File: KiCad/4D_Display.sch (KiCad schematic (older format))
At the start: 5 parts, among them J12 Display Serial Header, J4 V2 Display Ribbon Cable, Q3 MMBT3904

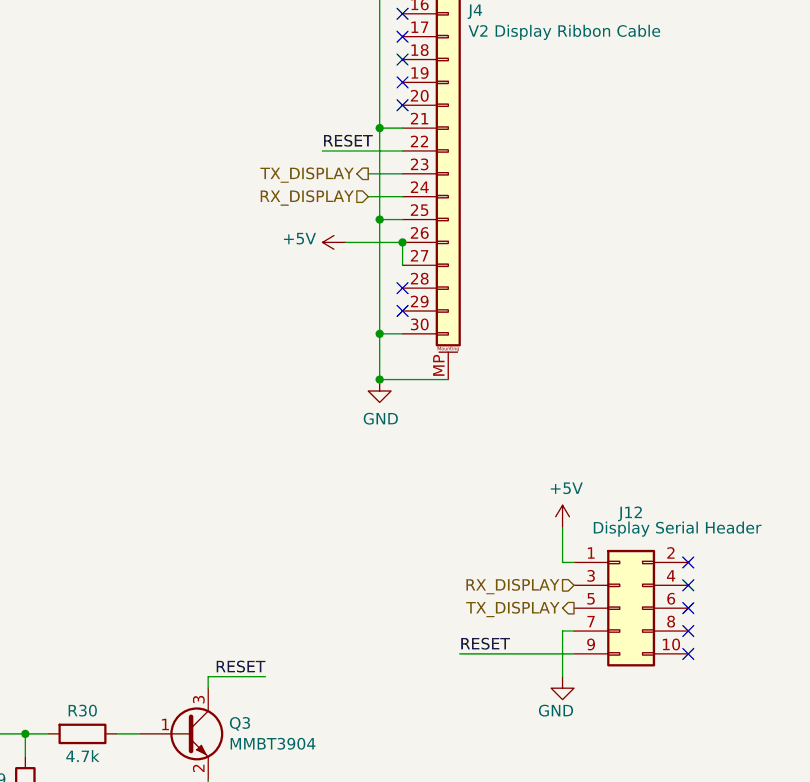
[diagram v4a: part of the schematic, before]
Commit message: Updating board to remove EXP1/EXP2
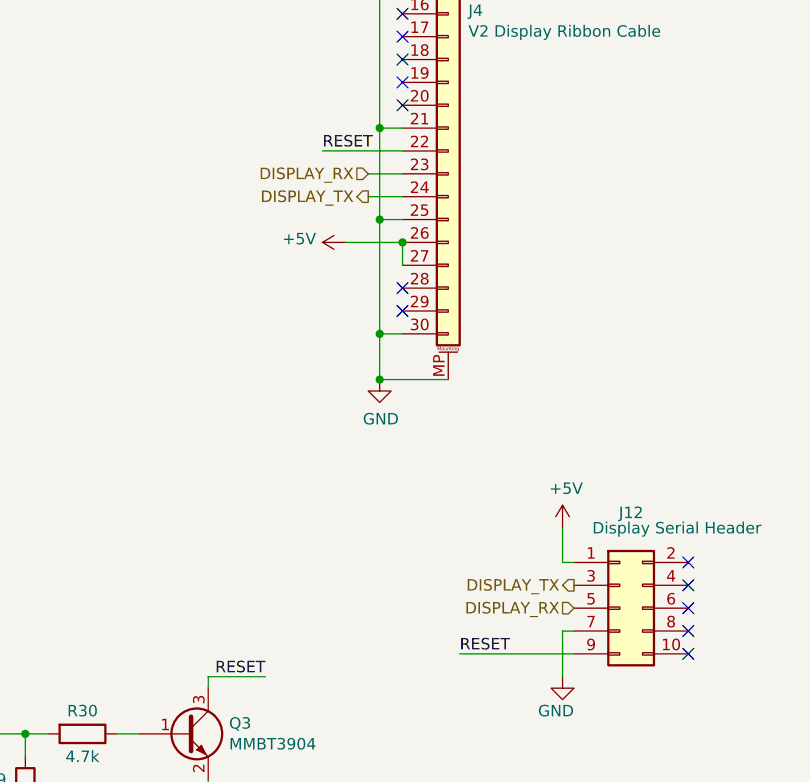
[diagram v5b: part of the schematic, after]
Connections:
- net RX_DISPLAY renamed DISPLAY_TX
- net TX_DISPLAY renamed DISPLAY_RX
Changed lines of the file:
@@
 Wire Wire Line
 	3550 6450 3550 6550
-Text HLabel 5150 5600 0    50   Input ~ 0
-RX_DISPLAY
-Text HLabel 5150 5700 0    50   Output ~ 0
-TX_DISPLAY
 Text HLabel 2350 6250 0    50   Input ~ 0
 RESET_DISPLAY
@@
 	0    -1   -1   0
 $EndComp
-Text HLabel 4250 3900 0    50   Input ~ 0
-RX_DISPLAY
-Text HLabel 4250 3800 0    50   Output ~ 0
-TX_DISPLAY
+Text HLabel 4250 3800 0    50   Input ~ 0
+DISPLAY_RX
+Text HLabel 4250 3900 0    50   Output ~ 0
+DISPLAY_TX
+Text HLabel 5150 5700 0    50   Input ~ 0
+DISPLAY_RX
+Text HLabel 5150 5600 0    50   Output ~ 0
+DISPLAY_TX
 $EndSCHEMATC

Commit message: current KiCad progress
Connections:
- net RESET_DISPLAY renamed DISPLAY_RESET
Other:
- note added: "Check: Display reset is now 3.3V,\nwill this still work on the N-channel mosfet?"
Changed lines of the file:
@@
 $Descr A4 11693 8268
 encoding utf-8
-Sheet 5 5
+Sheet 2 4
 Title ""
 Date ""
@@
 Wire Wire Line
 	3550 6450 3550 6550
-Text HLabel 2350 6250 0    50   Input ~ 0
-RESET_DISPLAY
 Wire Wire Line
 	2350 6250 2750 6250
@@
 	0    -1   -1   0
 $EndComp
-Text HLabel 4250 3800 0    50   Input ~ 0
+Text GLabel 2350 6250 0    50   Input ~ 0
+DISPLAY_RESET
+Text Notes 1750 5850 0    50   ~ 0
+Check: Display reset is now 3.3V,\nwill this still work on the N-channel mosfet?
+Text GLabel 4250 3800 0    50   Input ~ 0
 DISPLAY_RX
-Text HLabel 4250 3900 0    50   Output ~ 0
+Text GLabel 5150 5700 0    50   Input ~ 0
+DISPLAY_RX
+Text GLabel 5150 5600 0    50   Input ~ 0
 DISPLAY_TX
-Text HLabel 5150 5700 0    50   Input ~ 0
-DISPLAY_RX
-Text HLabel 5150 5600 0    50   Output ~ 0
+Text GLabel 4250 3900 0    50   Input ~ 0
 DISPLAY_TX
 $EndSCHEMATC
